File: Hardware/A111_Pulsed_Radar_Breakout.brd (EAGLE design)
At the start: 33 x 39.4 mm, 44 parts, among them J4 RASPBERRYPI-26-PIN-GPIO, U1 A111, U2 1.8V, U4 TXB0108DQSR, Y1 26MHz

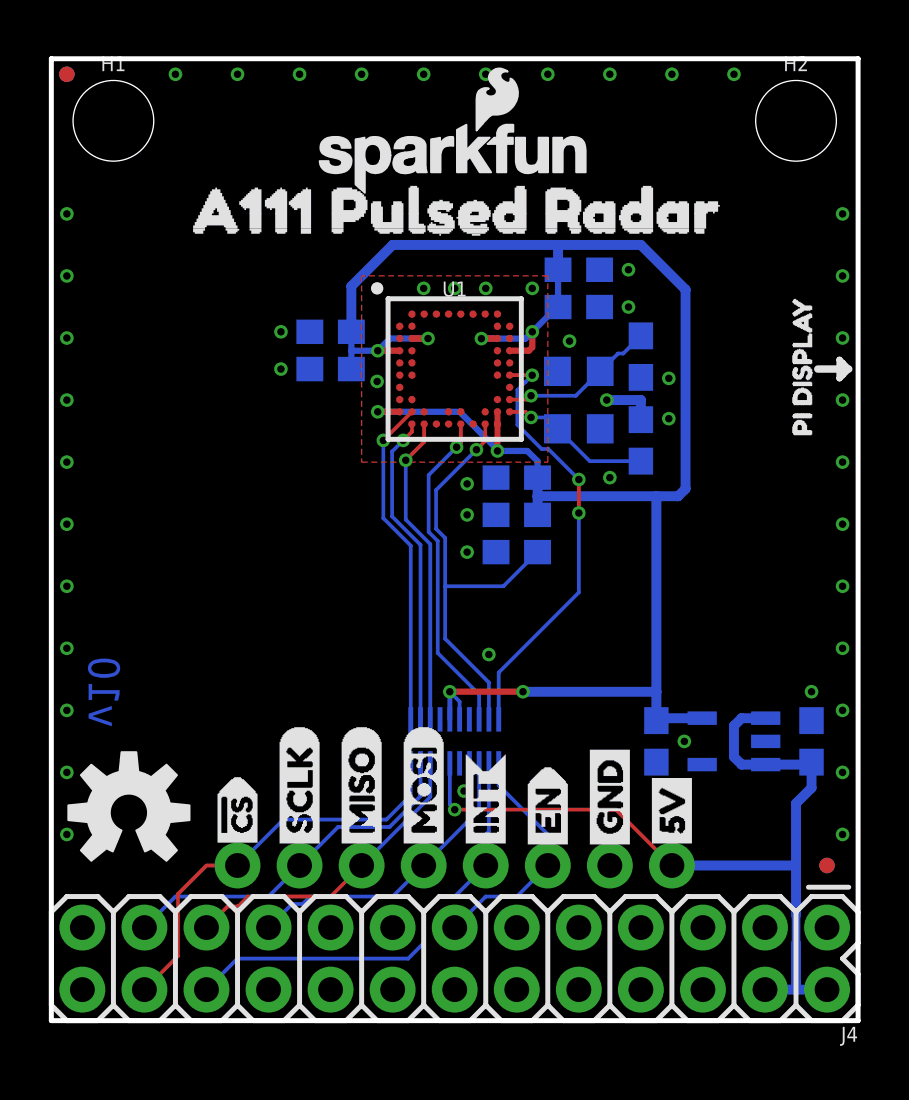
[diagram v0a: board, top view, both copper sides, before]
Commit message: Splits power to level translation so that it's at on a separate power bus (3.3V on Rasp Pi)
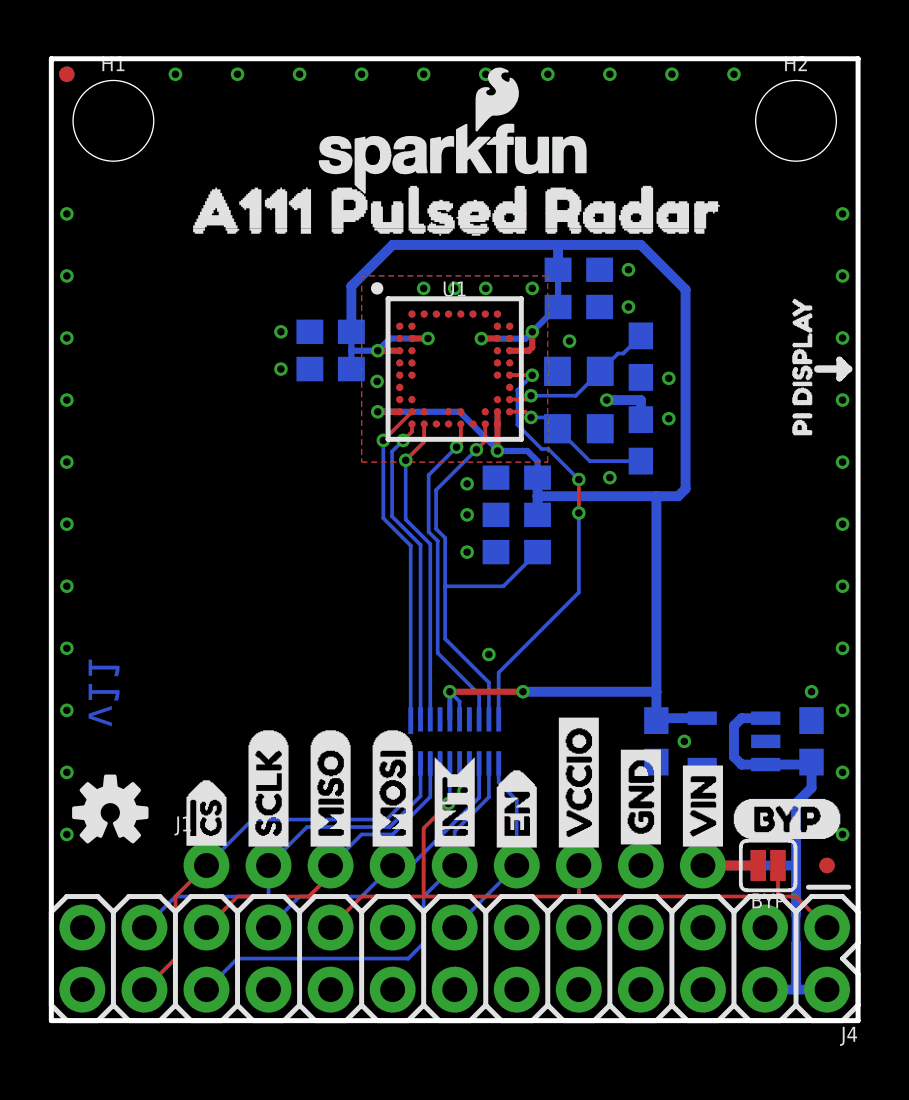
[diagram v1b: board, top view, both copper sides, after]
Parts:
- removed J2: (no value), SparkFun-Connectors:1X08_NO_SILK
- removed U$15: (no value), buzzard_labels:GND0
- added BYP: JUMPER-SMT_2_NO_SILK, SparkFun-Jumpers:SMT-JUMPER_2_NO_SILK
- added J1: (no value), SparkFun-Connectors:1X09_NO_SILK
- added U$19, U$20: (no value), buzzard_labels-x02:VCCIO1
- added U$21: (no value), buzzard_labels-x02:GND6
- added U$22: (no value), buzzard_labels-x02:VIN5
- LOGO2: value OSHW-LOGOM -> OSHW-LOGOS; device SparkFun-Aesthetics:OSHW-LOGO-M -> SparkFun-Aesthetics:OSHW-LOGO-S
- U$16: device buzzard_labels:5V1 -> buzzard_labels-x02:VIN0
- U$8: device buzzard_labels:5V1 -> SparkFun-Buzzard:BYP
- U2: value 1.8V -> AP2127K-1.8V
- moved U$8 2.85 mm to (27.8, 8.26), turned to 0 degrees
- moved U$16 1.28 mm to (26.7, 6.60), flipped to the top
- moved U$13 1.28 mm to (6.35, 6.48)
- moved U$17 1.28 mm to (6.35, 6.48)
- moved U$10 1.28 mm to (8.89, 6.60)
- moved U$11 1.28 mm to (11.4, 6.60)
- moved U$18 1.28 mm to (19.1, 6.60)
- moved U$2 1.28 mm to (8.89, 6.60)
- moved U$3 1.28 mm to (11.4, 6.60)
- moved U$4 1.28 mm to (14.0, 6.60)
- moved U$5 1.28 mm to (16.5, 6.60)
- moved U$6 1.28 mm to (19.1, 6.60)
- moved U$7 1.27 mm to (24.1, 6.73)
- moved LOGO2 0.76 mm to (2.41, 8.51)
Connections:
- removed net 5V: C9.1, J2.1, J4.2, J4.4, U2.1, U2.3, U4.16
- new net VCCIO: BYP.1, J1.7, J4.1, J4.17, U4.16
- new net VIN: BYP.2, C9.1, J1.9, J4.2, J4.4, U2.1, U2.3
- net !CS!_RPI: now also J1.1; no longer J2.8
- net ENABLE_RPI: now also J1.6; no longer J2.3
- net GND: now also J1.8; no longer J2.2
- net INTERRUPT_RPI: now also J1.5; no longer J2.4
- net MISO_RPI: now also J1.3; no longer J2.6
- net MOSI_RPI: now also J1.4; no longer J2.5
- net SCLK_RPI: now also J1.2; no longer J2.7
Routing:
- net 5V: track 35.1 -> 0.00 mm, vias 1 -> 0
- net VCCIO: track 0.00 -> 29.8 mm, vias 0 -> 1
- net VIN: track 0.00 -> 24.2 mm
- net ENABLE_RPI: track 9.87 -> 8.08 mm
- net SCLK_RPI: track 14.9 -> 15.6 mm
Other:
- board text added: "v11"
- board text removed: "v10"
